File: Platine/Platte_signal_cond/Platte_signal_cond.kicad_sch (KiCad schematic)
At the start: 16 parts, among them J1 Conn_01x06, J2 Conn_01x07_MountingPin

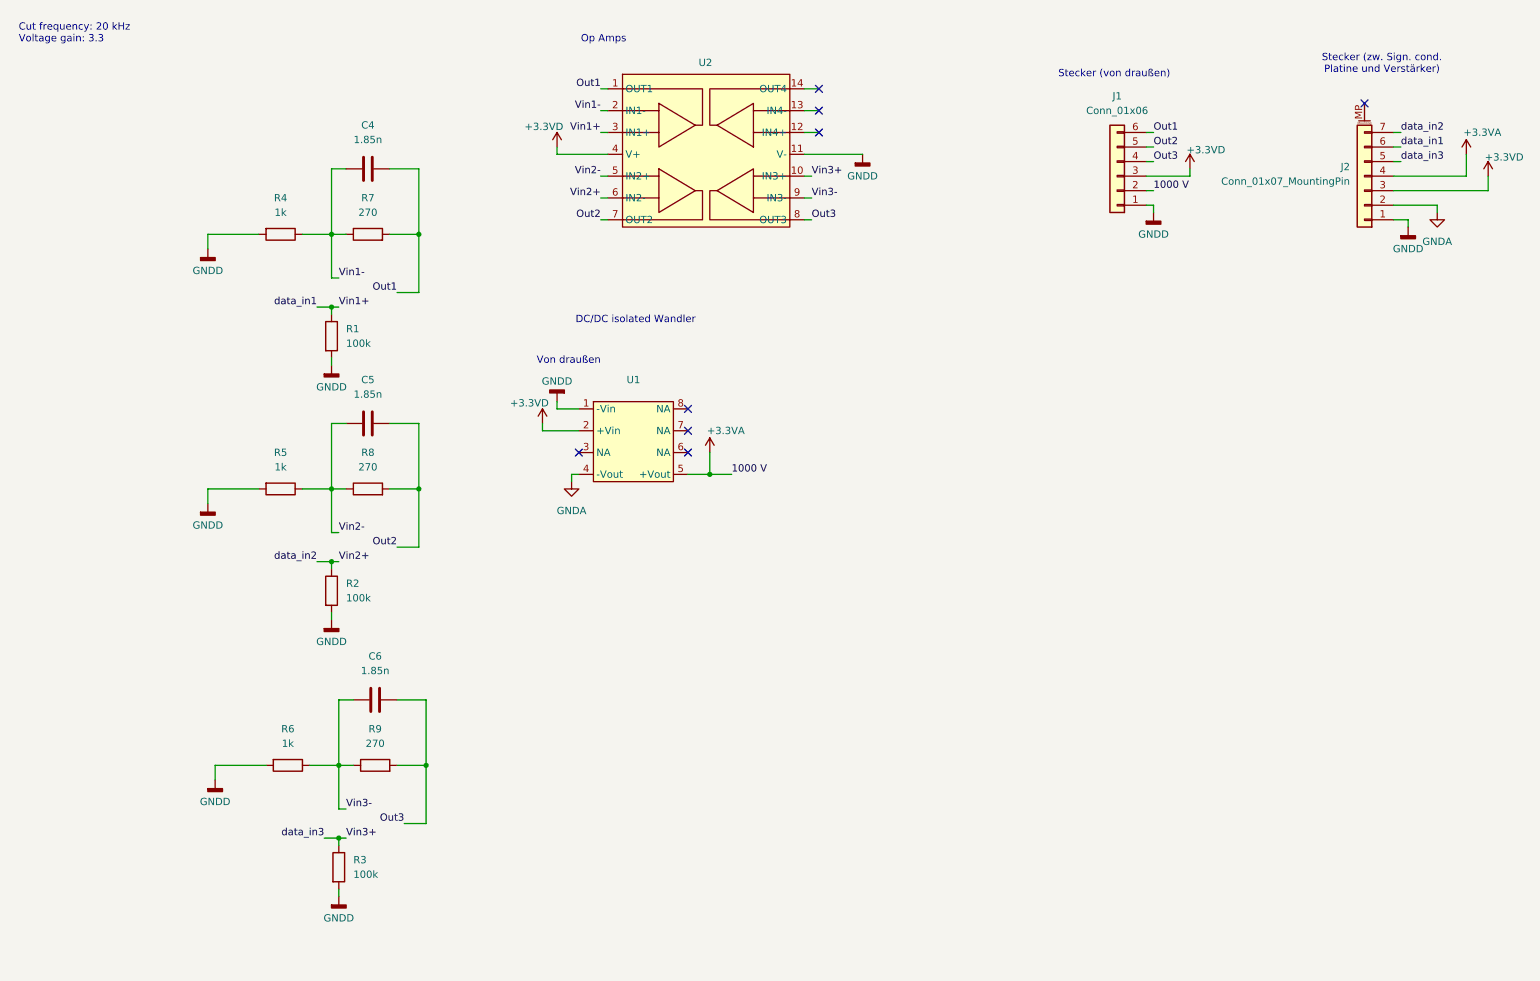
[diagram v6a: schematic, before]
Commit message: Final circuits designed. Plate PCB ready, signal cond PCB still in process
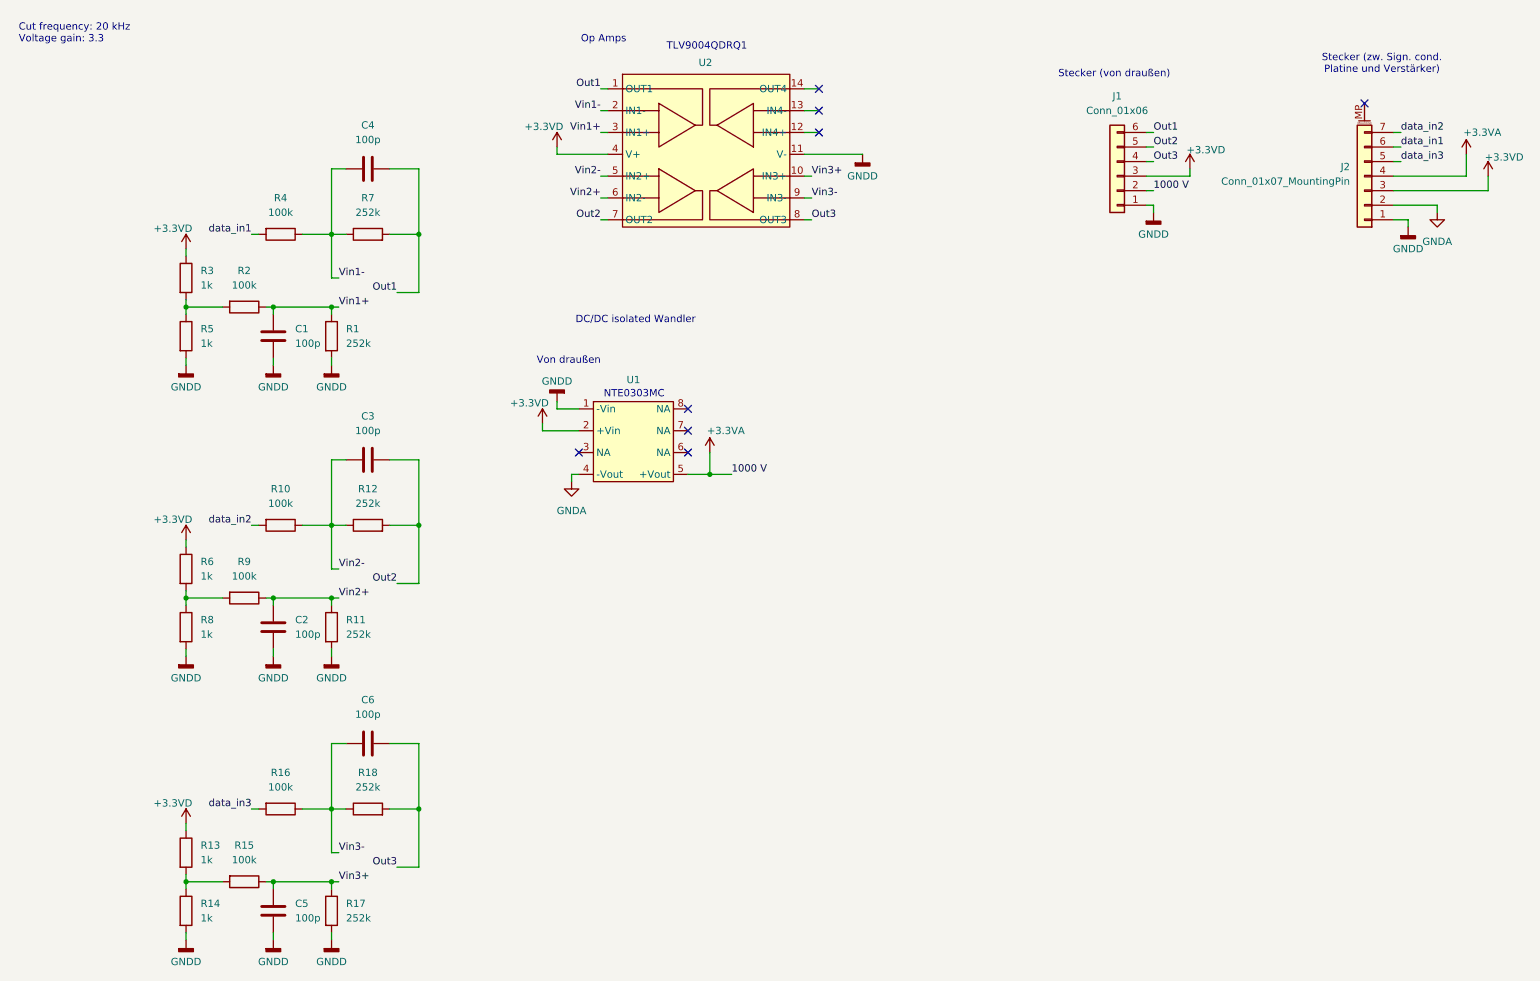
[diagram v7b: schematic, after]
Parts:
- added C1, C2, C3: 100p, Capacitor_SMD:C_0603_1608Metric_Pad1.08x0.95mm_HandSolder, symbol Device:C
- added R10, R15, R16: 100k, Resistor_SMD:R_0603_1608Metric_Pad0.98x0.95mm_HandSolder, symbol Device:R
- added R11, R12, R17, R18: 252k, Resistor_SMD:R_0603_1608Metric_Pad0.98x0.95mm_HandSolder, symbol Device:R
- added R13, R14: 1k, Resistor_SMD:R_0603_1608Metric_Pad0.98x0.95mm_HandSolder, symbol Device:R
- C4, C5, C6: value 1.85n -> 100p
- R1: value 100k -> 252k
- R3: value 100k -> 1k
- R4: value 1k -> 100k
- R7: value 270 -> 252k
- R8: value 270 -> 1k
- R9: value 270 -> 100k
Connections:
- net +3.3VD: now also R3.1, R6.1, R13.1
- net GNDD: now also C5.1, R8.2, C1.1, C2.1, R11.2, R14.2, R17.2; no longer R2.2, R3.2, R4.2, R6.2
- net Out1: now also C4.1; no longer C4.2
- net Out2: now also C3.1, R12.2; no longer C5.2, R8.2
- net Out3: now also C6.1, R18.2; no longer C6.2, R9.2
- net Vin1+: now also R2.1, C1.2; no longer J2.6 (Pin_6)
- net Vin1-: now also C4.2; no longer C4.1
- net Vin2+: now also R9.1, C2.2, R11.1; no longer J2.7 (Pin_7), R2.1
- net Vin2-: now also C3.2, R10.1, R12.1; no longer C5.1, R5.1, R8.1
- net Vin3+: now also C5.2, R15.1, R17.1; no longer J2.5 (Pin_5), R3.1
- net Vin3-: now also C6.2, R16.1, R18.1; no longer C6.1, R6.1, R9.1
- new net: R6.2, R8.1, R9.2
- new net: R13.2, R14.1, R15.2
- new net: R2.2, R3.2, R5.1
- new net data_in1: J2.6 (Pin_6), R4.2
- new net data_in2: J2.7 (Pin_7), R10.2
- new net data_in3: J2.5 (Pin_5), R16.2
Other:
- note added: "NTE0303MC"
- note added: "TLV9004QDRQ1"
- moved on the sheet: C4

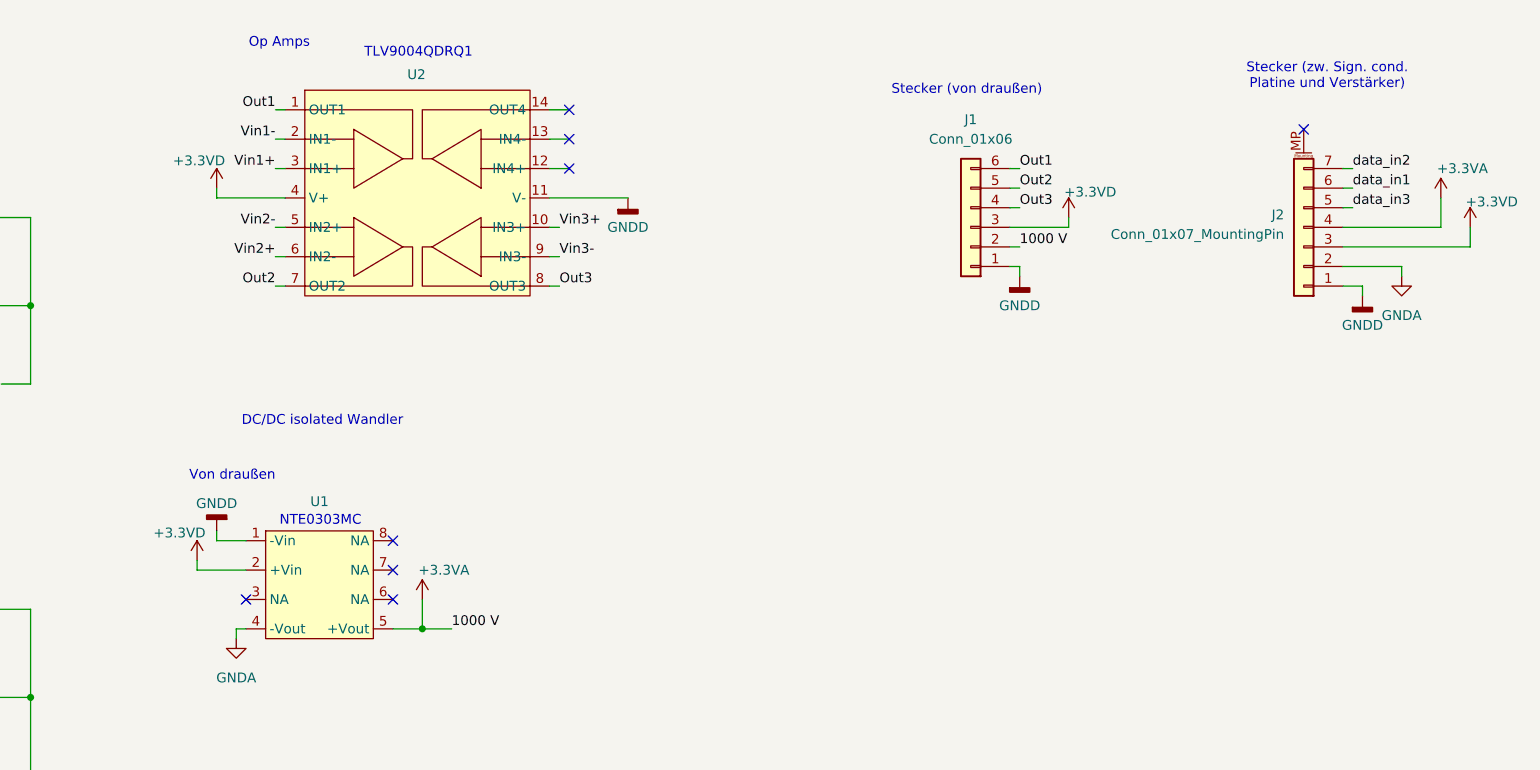
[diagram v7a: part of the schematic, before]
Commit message: Made a few changes to PCBs and schematics
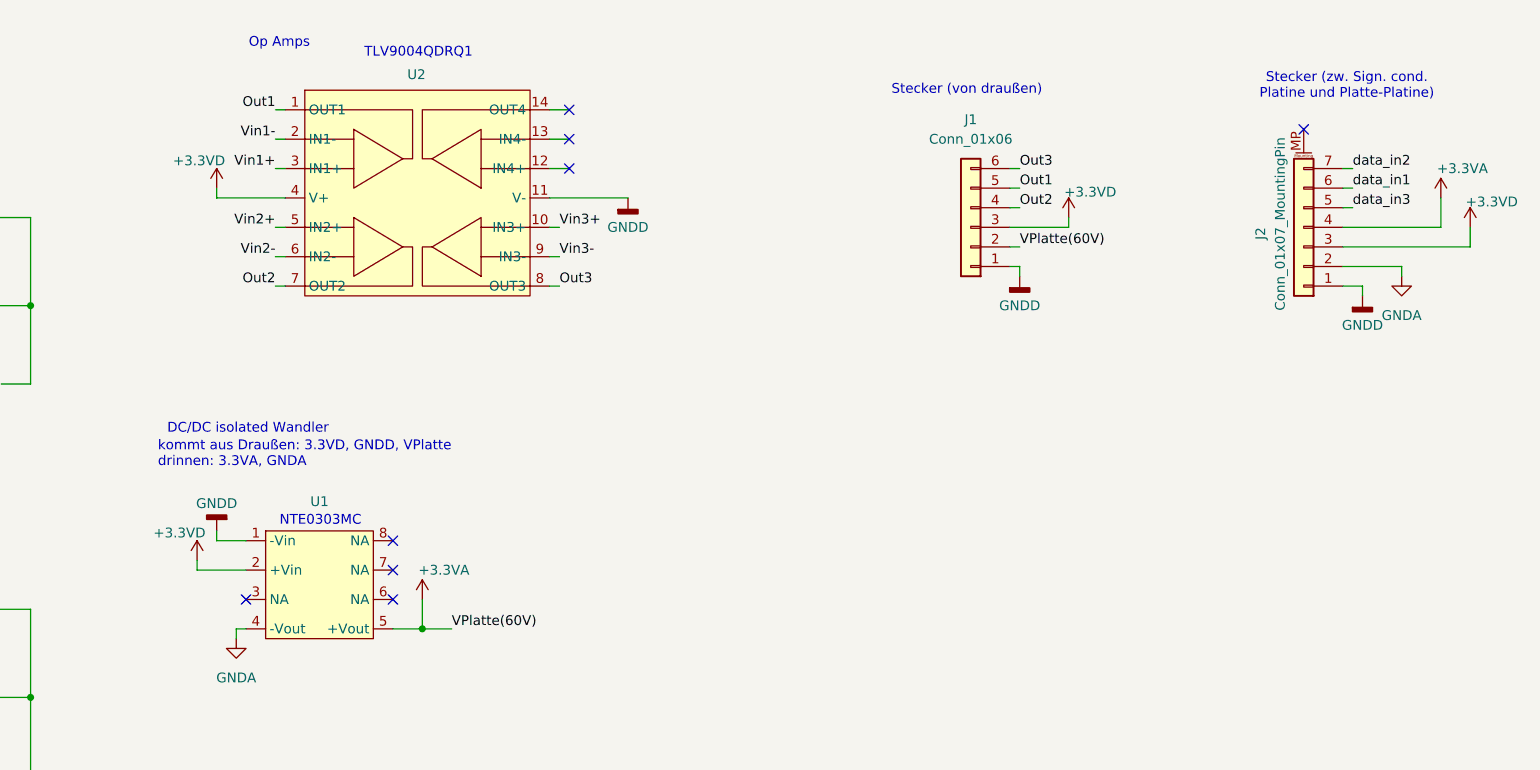
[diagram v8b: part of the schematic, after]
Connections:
- net Out1: now also J1.5 (Pin_5); no longer J1.6 (Pin_6)
- net Out2: now also J1.4 (Pin_4); no longer J1.5 (Pin_5)
- net Out3: now also J1.6 (Pin_6); no longer J1.4 (Pin_4)
- net Vin2+: now also U2.5 (IN2+); no longer U2.6 (IN2-)
- net Vin2-: now also U2.6 (IN2-); no longer U2.5 (IN2+)
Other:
- note added: "Stecker (zw. Sign. cond. Platine und Platte-Platine)"
- note added: "kommt aus Draußen: 3.3VD, GNDD, VPlatte drinnen: 3.3VA, GNDA"
- note removed: "Stecker (zw. Sign. cond. Platine und Verstärker)"
- note removed: "Von draußen"
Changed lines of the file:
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@@
+	(wire
+		(pts
+			(xy 214.63 35.56) (xy 215.9 35.56)
+		)
+		(stroke
+			(width 0)
+			(type default)
+		)
+	)
 	(wire
 		(pts
@@
 	(wire
 		(pts
-			(xy 214.63 35.56) (xy 215.9 35.56)
-		)
-		(stroke
-			(width 0)
-			(type default)
-		)
-	)
-	(wire
-		(pts
 			(xy 257.81 38.1) (xy 259.08 38.1)
 		)
@@
 	(wire
 		(pts
+			(xy 119.38 43.18) (xy 120.65 43.18)
+		)
+		(stroke
+			(width 0)
+			(type default)
+		)
+	)
+	(wire
+		(pts
 			(xy 83.82 163.83) (xy 87.63 163.83)
 		)
@@
 	(wire
 		(pts
-			(xy 119.38 43.18) (xy 120.65 43.18)
-		)
-		(stroke
-			(width 0)
-			(type default)
-		)
-	)
-	(wire
-		(pts
 			(xy 87.63 142.24) (xy 87.63 153.67)
 		)
@@
 	(wire
 		(pts
+			(xy 214.63 40.64) (xy 215.9 40.64)
+		)
+		(stroke
+			(width 0)
+			(type default)
+		)
+	)
+	(wire
+		(pts
 			(xy 72.39 116.84) (xy 73.66 116.84)
 		)
@@
 	(wire
 		(pts
+			(xy 214.63 38.1) (xy 215.9 38.1)
+		)
+		(stroke
+			(width 0)
+			(type default)
+		)
+	)
+	(wire
+		(pts
 			(xy 154.94 27.94) (xy 157.48 27.94)
 		)
@@
 	(wire
 		(pts
+			(xy 119.38 46.99) (xy 120.65 46.99)
+		)
+		(stroke
+			(width 0)
+			(type default)
+		)
+	)
+	(wire
+		(pts
 			(xy 257.81 50.8) (xy 260.35 50.8)
 		)
@@
 	(wire
 		(pts
-			(xy 214.63 38.1) (xy 215.9 38.1)
-		)
-		(stroke
-			(width 0)
-			(type default)
-		)
-	)
-	(wire
-		(pts
 			(xy 257.81 45.72) (xy 274.32 45.72)
 		)
@@
 	(wire
 		(pts
-			(xy 214.63 40.64) (xy 215.9 40.64)
-		)
-		(stroke
-			(width 0)
-			(type default)
-		)
-	)
-	(wire
-		(pts
 			(xy 82.55 41.91) (xy 87.63 41.91)
 		)
@@
 	(wire
 		(pts
-			(xy 119.38 46.99) (xy 120.65 46.99)
-		)
-		(stroke
-			(width 0)
-			(type default)
-		)
-	)
-	(wire
-		(pts
 			(xy 72.39 161.29) (xy 73.66 161.29)
 		)
@@
 		)
 	)
-	(text "Von draußen"
+	(text "kommt aus Draußen: 3.3VD, GNDD, VPlatte\ndrinnen: 3.3VA, GNDA"
 		(exclude_from_sim no)
-		(at 113.792 75.438 0)
-		(effects
-			(font
-				(size 1.27 1.27)
-			)
+		(at 104.14 72.644 0)
+		(effects
+			(font
+				(size 1.27 1.27)
+			)
+			(justify left)
 		)
 	)
@@
 	(text "DC/DC isolated Wandler"
 		(exclude_from_sim no)
-		(at 125.476 68.326 0)
+		(at 115.824 69.342 0)
 		(effects
 			(font
@@
 		)
 	)
-	(text "Stecker (zw. Sign. cond.\nPlatine und Verstärker)"
+	(text "Stecker (zw. Sign. cond.\nPlatine und Platte-Platine)"
 		(exclude_from_sim no)
-		(at 255.778 23.622 0)
+		(at 258.318 24.892 0)
 		(effects
 			(font
@@
 	)
 	(label "Vin2+"
-		(at 119.38 46.99 180)
+		(at 119.38 43.18 180)
 		(fields_autoplaced yes)
 		(effects
@@
 	)
 	(label "Vin2-"
-		(at 119.38 43.18 180)
+		(at 119.38 46.99 180)
 		(fields_autoplaced yes)
 		(effects
@@
 		)
 	)
-	(label "1000 V"
+	(label "VPlatte(60V)"
 		(at 215.9 45.72 0)
 		(fields_autoplaced yes)
@@
 	)
 	(label "Out2"
+		(at 215.9 40.64 0)
+		(fields_autoplaced yes)
+		(effects
+			(font
+				(size 1.27 1.27)
+			)
+			(justify left bottom)
+		)
+	)
+	(label "Out1"
 		(at 215.9 38.1 0)
-		(fields_autoplaced yes)
-		(effects
-			(font
-				(size 1.27 1.27)
-			)
-			(justify left bottom)
-		)
-	)
-	(label "Out1"
-		(at 215.9 35.56 0)
 		(fields_autoplaced yes)
 		(effects
@@
 		)
 	)
-	(label "1000 V"
+	(label "VPlatte(60V)"
 		(at 142.24 95.25 0)
 		(fields_autoplaced yes)
@@
 	)
 	(label "Out3"
-		(at 215.9 40.64 0)
+		(at 215.9 35.56 0)
 		(fields_autoplaced yes)
 		(effects
@@
 		(on_board yes)
 		(dnp no)
-		(fields_autoplaced yes)
 		(property "Reference" "J2"
-			(at 250.19 41.5543 0)
+			(at 247.142 43.18 90)
 			(effects
 				(font
@@
 		)
 		(property "Value" "Conn_01x07_MountingPin"
-			(at 250.19 44.0943 0)
-			(effects
-				(font
+			(at 249.682 31.496 90)
+			(effects
+				(font
